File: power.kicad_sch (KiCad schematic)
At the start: 22 parts

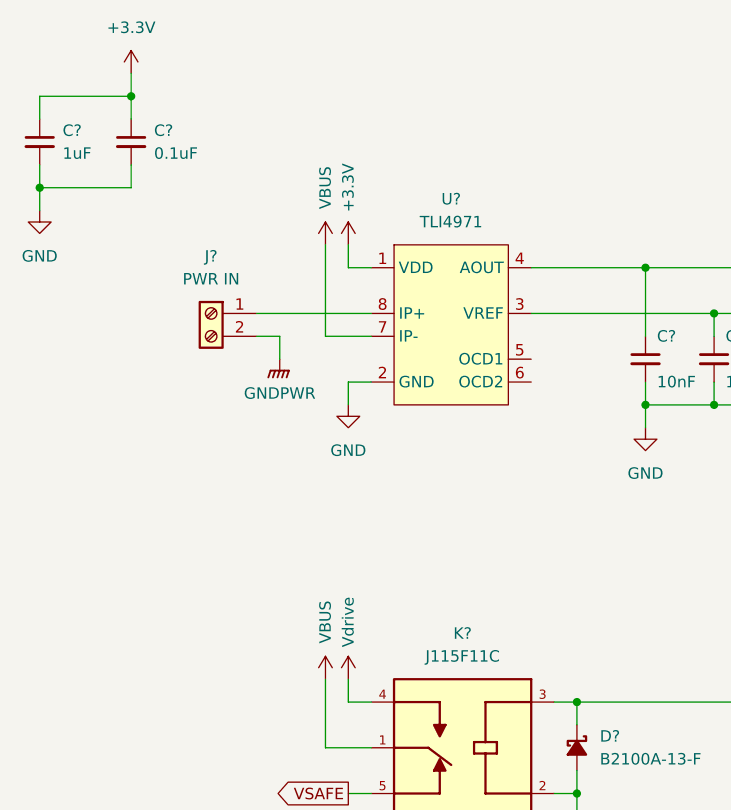
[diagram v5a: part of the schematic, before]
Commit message: Added hot-side supply protection
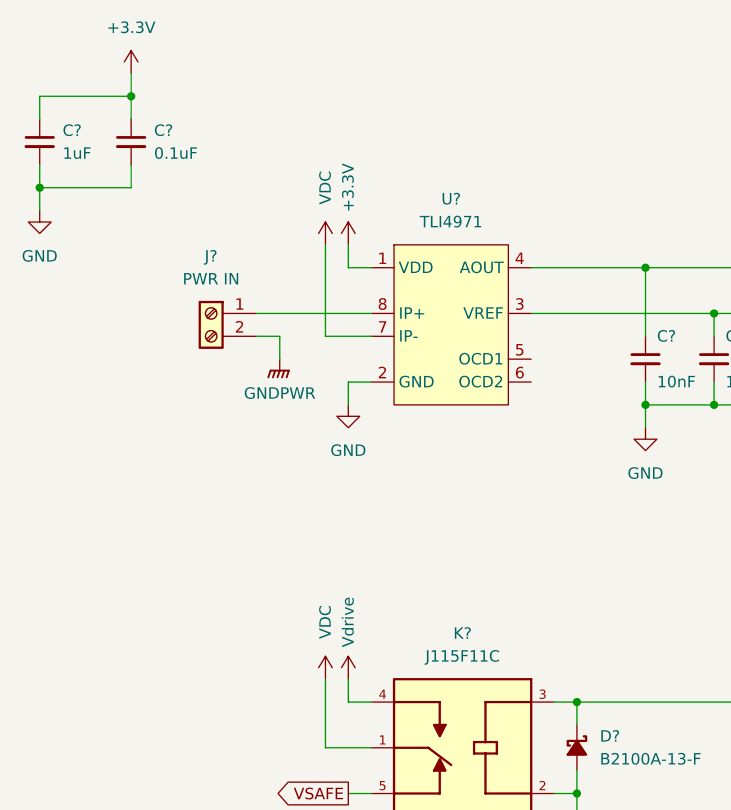
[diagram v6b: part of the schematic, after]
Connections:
- net VBUS renamed VDC

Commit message: Reorganizing schematic
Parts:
- C? (x2): value 10nF -> 6.8nF
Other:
- note added: "20-28V acceptable input"
- moved on the sheet: C?, D?, J?, K?, Q?, R?, U?

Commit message: More reorganizing
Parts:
- J?: value ACT HOT -> ACT ARMED
- J?: value ACT COLD -> ACT DISARMED
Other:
- note added: "Beacons"
- note added: "Power In and Current Sense"
- note added: "Safing Relay and Arming Logic"
- moved on the sheet: C?, D?, J?, K?, Q?, R?, U?
